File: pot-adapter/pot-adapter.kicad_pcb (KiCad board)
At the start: 2 copper layers, 15.2 x 22.9 mm, 3 parts, among them J1 Conn_01x03_Male, J2 Conn_01x03_Male

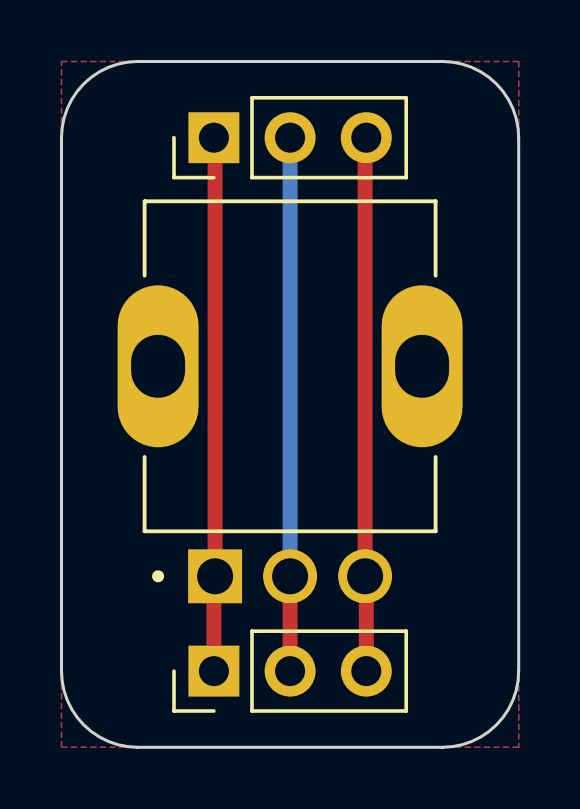
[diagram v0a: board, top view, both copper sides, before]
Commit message: Pot Adapter v1rev1
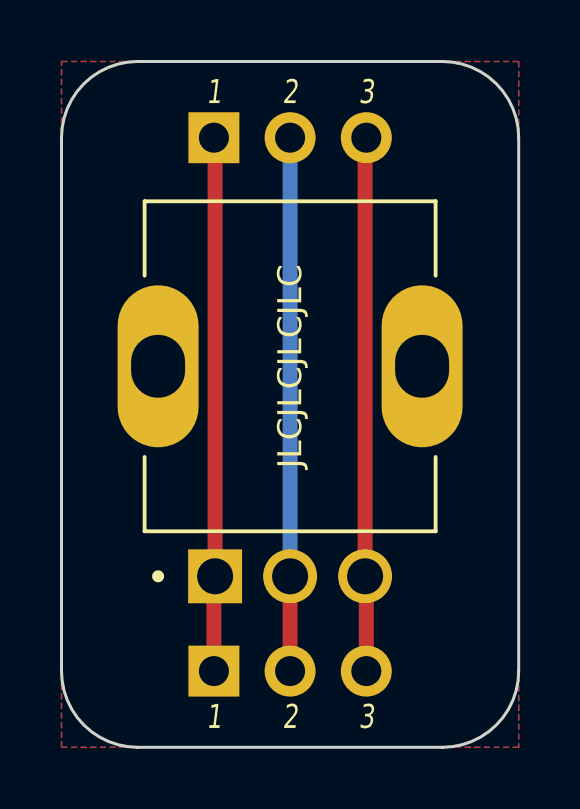
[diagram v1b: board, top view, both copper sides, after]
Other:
- board text added: "1"
- board text added: "2"
- board text added: "3"
- board text added: "JLCJLCJLCJLC"
- board text added: "v1rev1"
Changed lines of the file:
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@@
       (effects (font (size 1 1) (thickness 0.15)))
     )
-    (fp_line (start -1.33 1.27) (end -1.33 6.41) (layer "F.SilkS") (width 0.12))
-    (fp_line (start -1.33 0) (end -1.33 -1.33) (layer "F.SilkS") (width 0.12))
-    (fp_line (start -1.33 1.27) (end 1.33 1.27) (layer "F.SilkS") (width 0.12))
-    (fp_line (start -1.33 6.41) (end 1.33 6.41) (layer "F.SilkS") (width 0.12))
-    (fp_line (start 1.33 1.27) (end 1.33 6.41) (layer "F.SilkS") (width 0.12))
-    (fp_line (start -1.33 -1.33) (end 0 -1.33) (layer "F.SilkS") (width 0.12))
     (fp_line (start -1.8 6.85) (end 1.8 6.85) (layer "F.CrtYd") (width 0.05))
     (fp_line (start 1.8 6.85) (end 1.8 -1.8) (layer "F.CrtYd") (width 0.05))
@@
     (fp_line (start -0.635 -1.27) (end 1.27 -1.27) (layer "F.Fab") (width 0.1))
     (fp_line (start -1.27 -0.635) (end -0.635 -1.27) (layer "F.Fab") (width 0.1))
+    (fp_line (start -1.33 1.27) (end -1.33 6.41) (layer "User.1") (width 0.12))
+    (fp_line (start -1.33 0) (end -1.33 -1.33) (layer "User.1") (width 0.12))
+    (fp_line (start -1.33 1.27) (end 1.33 1.27) (layer "User.1") (width 0.12))
+    (fp_line (start -1.33 6.41) (end 1.33 6.41) (layer "User.1") (width 0.12))
+    (fp_line (start 1.33 1.27) (end 1.33 6.41) (layer "User.1") (width 0.12))
+    (fp_line (start -1.33 -1.33) (end 0 -1.33) (layer "User.1") (width 0.12))
     (pad "1" thru_hole rect (at 0 0 90) (size 1.7 1.7) (drill 1) (layers *.Cu *.Mask)
       (net 1 "/pin1") (pinfunction "Pin_1") (pintype "passive"))
@@
       (effects (font (size 1 1) (thickness 0.15)))
     )
-    (fp_line (start -1.33 1.27) (end -1.33 6.41) (layer "F.SilkS") (width 0.12))
-    (fp_line (start -1.33 6.41) (end 1.33 6.41) (layer "F.SilkS") (width 0.12))
-    (fp_line (start 1.33 1.27) (end 1.33 6.41) (layer "F.SilkS") (width 0.12))
-    (fp_line (start -1.33 0) (end -1.33 -1.33) (layer "F.SilkS") (width 0.12))
-    (fp_line (start -1.33 1.27) (end 1.33 1.27) (layer "F.SilkS") (width 0.12))
-    (fp_line (start -1.33 -1.33) (end 0 -1.33) (layer "F.SilkS") (width 0.12))
     (fp_line (start 1.8 -1.8) (end -1.8 -1.8) (layer "F.CrtYd") (width 0.05))
     (fp_line (start 1.8 6.85) (end 1.8 -1.8) (layer "F.CrtYd") (width 0.05))
@@
     (fp_line (start -1.27 -0.635) (end -0.635 -1.27) (layer "F.Fab") (width 0.1))
     (fp_line (start 1.27 -1.27) (end 1.27 6.35) (layer "F.Fab") (width 0.1))
+    (fp_line (start -1.33 1.27) (end -1.33 6.41) (layer "User.1") (width 0.12))
+    (fp_line (start -1.33 6.41) (end 1.33 6.41) (layer "User.1") (width 0.12))
+    (fp_line (start 1.33 1.27) (end 1.33 6.41) (layer "User.1") (width 0.12))
+    (fp_line (start -1.33 0) (end -1.33 -1.33) (layer "User.1") (width 0.12))
+    (fp_line (start -1.33 1.27) (end 1.33 1.27) (layer "User.1") (width 0.12))
+    (fp_line (start -1.33 -1.33) (end 0 -1.33) (layer "User.1") (width 0.12))
     (pad "1" thru_hole rect (at 0 0 90) (size 1.7 1.7) (drill 1) (layers *.Cu *.Mask)
       (net 1 "/pin1") (pinfunction "Pin_1") (pintype "passive"))
@@
   (gr_arc (start 104.14 111.76) (mid 104.883949 109.963949) (end 106.68 109.22) (layer "Edge.Cuts") (width 0.1))
   (gr_line (start 106.68 109.22) (end 116.84 109.22) (layer "Edge.Cuts") (width 0.1))
+  (gr_text "v1rev1" (at 111.76 119.38) (layer "B.SilkS")
+    (effects (font (size 0.9 0.9) (thickness 0.15)) (justify mirror))
+  )
+  (gr_text "1" (at 109.22 131.064) (layer "F.SilkS")
+    (effects (font (size 0.8 0.6) (thickness 0.12) italic))
+  )
+  (gr_text "2" (at 111.76 131.064) (layer "F.SilkS")
+    (effects (font (size 0.8 0.6) (thickness 0.12) italic))
+  )
+  (gr_text "3" (at 114.3 131.064) (layer "F.SilkS")
+    (effects (font (size 0.8 0.6) (thickness 0.12) italic))
+  )
+  (gr_text "3" (at 114.3 110.236) (layer "F.SilkS")
+    (effects (font (size 0.8 0.6) (thickness 0.12) italic))
+  )
+  (gr_text "1" (at 109.22 110.236) (layer "F.SilkS")
+    (effects (font (size 0.8 0.6) (thickness 0.12) italic))
+  )
+  (gr_text "JLCJLCJLCJLC" (at 111.76 119.38 90) (layer "F.SilkS")
+    (effects (font (size 0.8 0.8) (thickness 0.15)))
+  )
+  (gr_text "2" (at 111.76 110.236) (layer "F.SilkS")
+    (effects (font (size 0.8 0.6) (thickness 0.12) italic))
+  )
   (segment (start 109.22 129.54) (end 109.22 126.42) (width 0.5) (layer "F.Cu") (net 1))
   (segment (start 109.26 126.38) (end 109.26 111.8) (width 0.5) (layer "F.Cu") (net 1))
